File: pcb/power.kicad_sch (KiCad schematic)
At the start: 22 parts, among them U1 74LVC1G08, U12 TPS2121RUXR, U13 TPS2121RUXR, U14 TPS2121RUXR

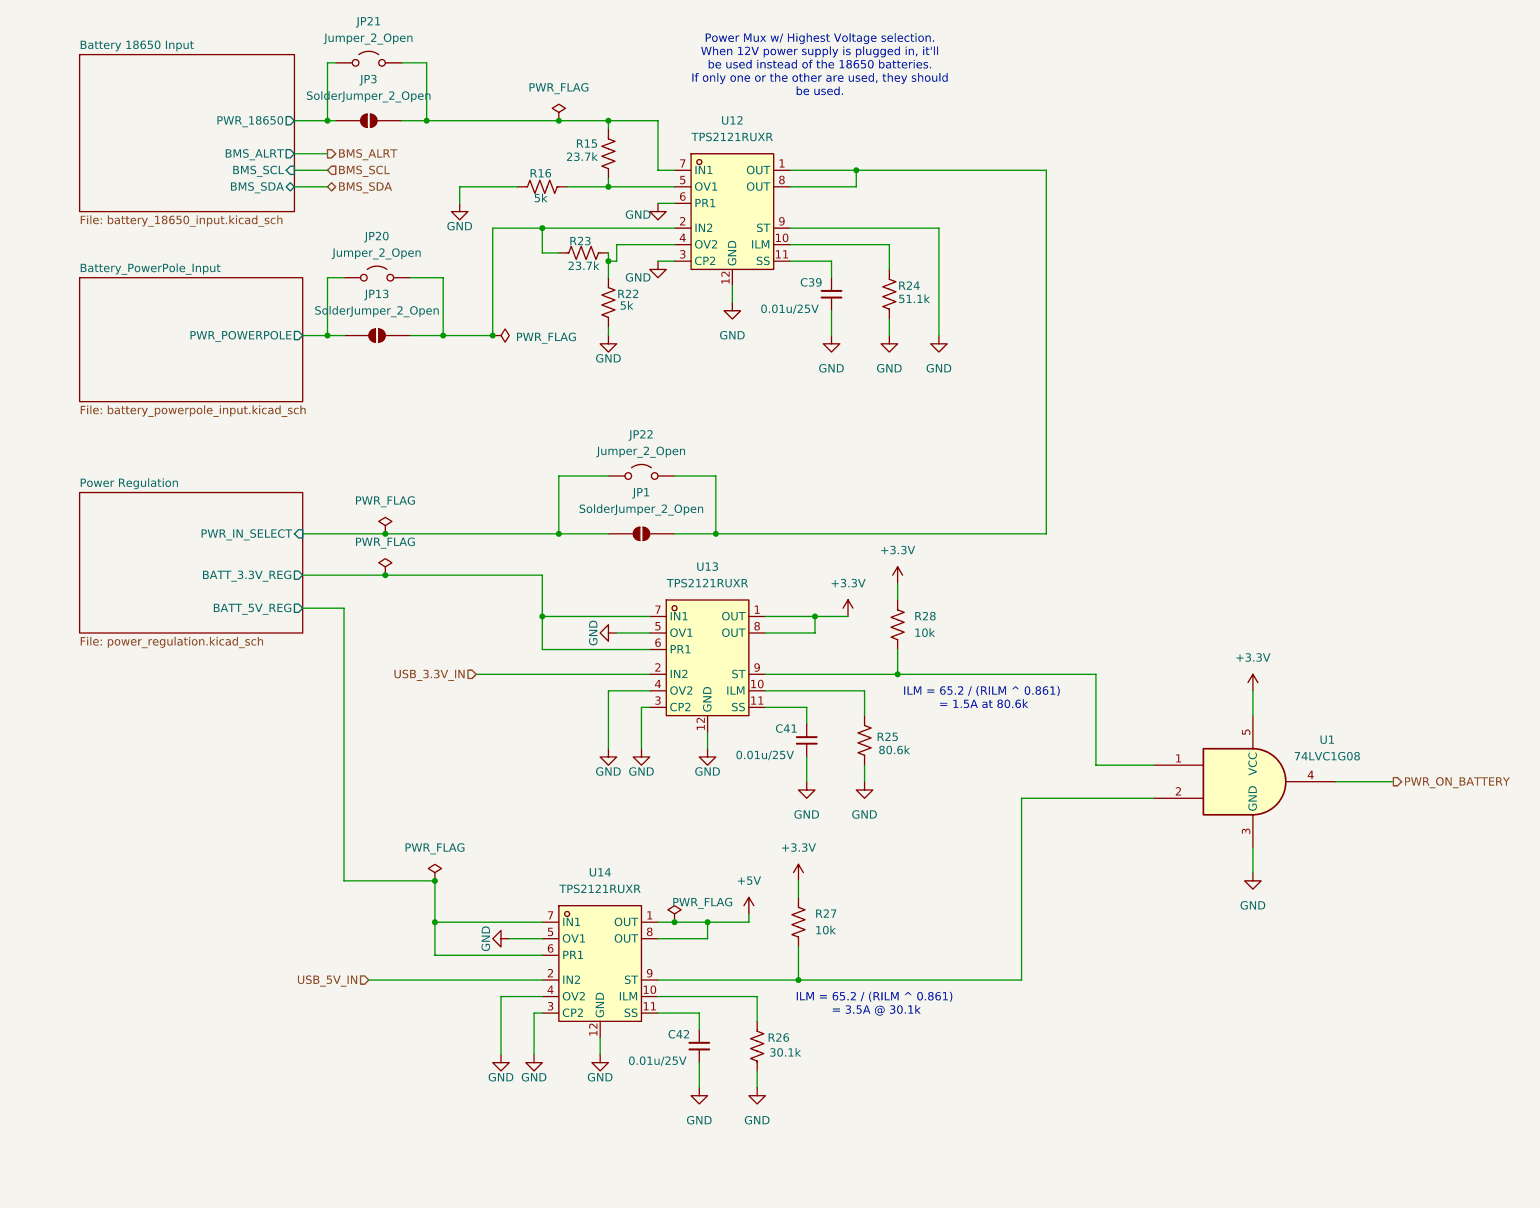
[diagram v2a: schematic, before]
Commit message: Full re-annotation, BOM audit fixes, Stage-1 ILM resize, and PCB reset
Schematic: re-annotated reference designators project-wide (3rd pass) --
every real component's designator has shifted since the last commit.
Fixed BOM gaps found by the fresh audit: U13 (CH340C) sourcing fields,
R7's Manf typo (YAGE -> YAGEO), R5/R8/R14 missing LCSC Part#s, and
normalized U1/U2/U3 (TPS2121RUXR) field names from easyeda2kicad's
defaults (Manufacturer/LCSC Part) to this project's convention
(Manf/LCSC Part #). Resized Stage 1's ILM resistor (R8) from 51.1k to
30.1k -- the prior value undersized the current limit for carrying both
downstream rails' combined battery-side current.

pcb/foxhunt1.kicad_pcb: cleared all footprints. No board layout has
started yet; this reflects that accurately rather than carrying stale
placements from before the schematic settled.

_agent_tasks/bom_property_audit.md: new reusable playbook for this BOM
audit (method, standing exceptions, reporting format), so future passes
don't have to re-derive the approach each time.

_docs/sourcing/task1_lcsc_crossreference.md: replaced stale results
(referencing pre-renumbering designators) with the current audit's
findings. One open item remains: the current-sense shunt's footprint
implies Vishay pad geometry but the sourced part is Milliohm-brand,
needs physical verification before fab.

Co-Authored-By: Claude Sonnet 5 <noreply@anthropic.com>
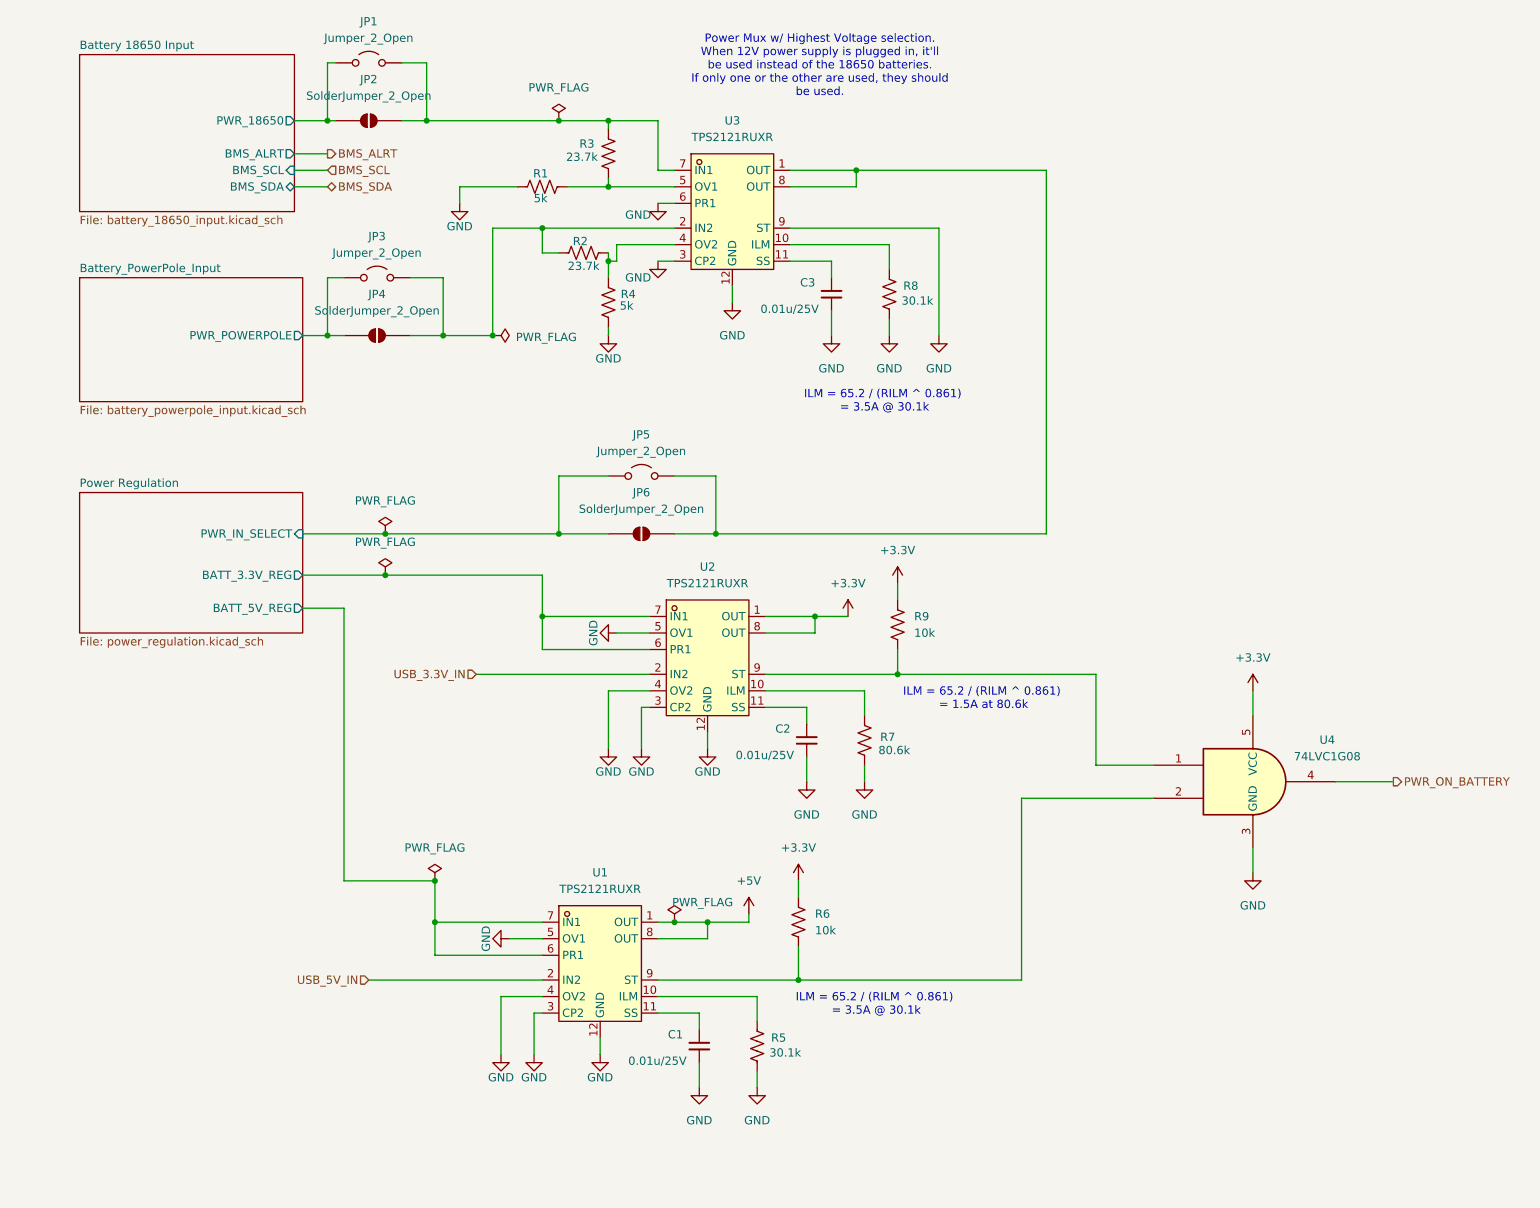
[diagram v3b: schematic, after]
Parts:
- removed R24: 51.1k, Resistor_SMD:R_0201_0603Metric, symbol Device:R_US
- added R8: 30.1k, Resistor_SMD:R_0603_1608Metric, symbol Device:R_US
- JP1: renamed from JP21; footprint (none) -> TestPoint:TestPoint_2Pads_Pitch2.54mm_Drill0.8mm
- JP3: renamed from JP20; footprint (none) -> TestPoint:TestPoint_2Pads_Pitch2.54mm_Drill0.8mm
- JP5: renamed from JP22; footprint (none) -> TestPoint:TestPoint_2Pads_Pitch2.54mm_Drill0.8mm
- R5: renamed from R26; footprint Resistor_SMD:R_0201_0603Metric -> Resistor_SMD:R_0603_1608Metric; LCSC Part # (none) -> C137745; MPN (none) -> RC0603FR-0730K1L; Manf YAGE -> YAGEO
- R7: renamed from R25; footprint Resistor_SMD:R_0201_0603Metric -> Resistor_SMD:R_0603_1608Metric; LCSC Part # (none) -> C862291; MPN (none) -> RT0603BRE0780K6L; Manf YAGE -> YAGEO
- U1: renamed from U14; LCSC Part C485916 -> (none); LCSC Part # (none) -> C485916; Manf (none) -> TI; Manufacturer TI -> (none)
- U2: renamed from U13; LCSC Part C485916 -> (none); LCSC Part # (none) -> C485916; Manf (none) -> TI; Manufacturer TI -> (none)
- U3: renamed from U12; LCSC Part C485916 -> (none); LCSC Part # (none) -> C485916; Manf (none) -> TI; Manufacturer TI -> (none)
- renumbered C42 to C1, C41 to C2, C39 to C3, JP3 to JP2, JP13 to JP4, JP1 to JP6, R16 to R1, R23 to R2, R15 to R3, R22 to R4, R27 to R6, R28 to R9, U1 to U4
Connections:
- net GND: now also R8.1
- net at U3.10 (ILM): now also R8.2

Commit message: Add VRAW soft-latch power switch and MCU/RTC wake network
- Q5 (AO3407A P-FET) gates VRAW into Power Regulation, gate driven by
  a shared active-low wake node (button SW3, RTC_PWR_INTERRUPT,
  MCU_OUT_PWR_LATCH) pulled up to VRAW through 1M R29
- Q6 (BSS138) on the mcu-esp32 sheet lets GPIO48 hold the latch from
  a 3.3V-safe domain without exposing the MCU to VRAW voltage
- JP5/JP6 bench-isolation jumpers in the VRAW-gated path, bridged via
  new VRAW_GATED net label into Power Regulation's PWR_IN_SELECT
- JP24 lets USB be excluded from the TPS2121 power muxes for bench
  testing the sleep/wake cycle while still connected over USB-C
- Added blank Peripherals sheet (mcu-esp32 child) with RTC-facing
  pins stubbed and wired at the root, ready for the PCF8563 circuit
- regulation.md updated for the final 6.67V/4.78V intermediate
  voltages and matched-tolerance thin-film feedback dividers
- open_items.md: added power-off path as a follow-up (latch only
  handles power-on today)

Co-Authored-By: Claude Sonnet 5 <noreply@anthropic.com>
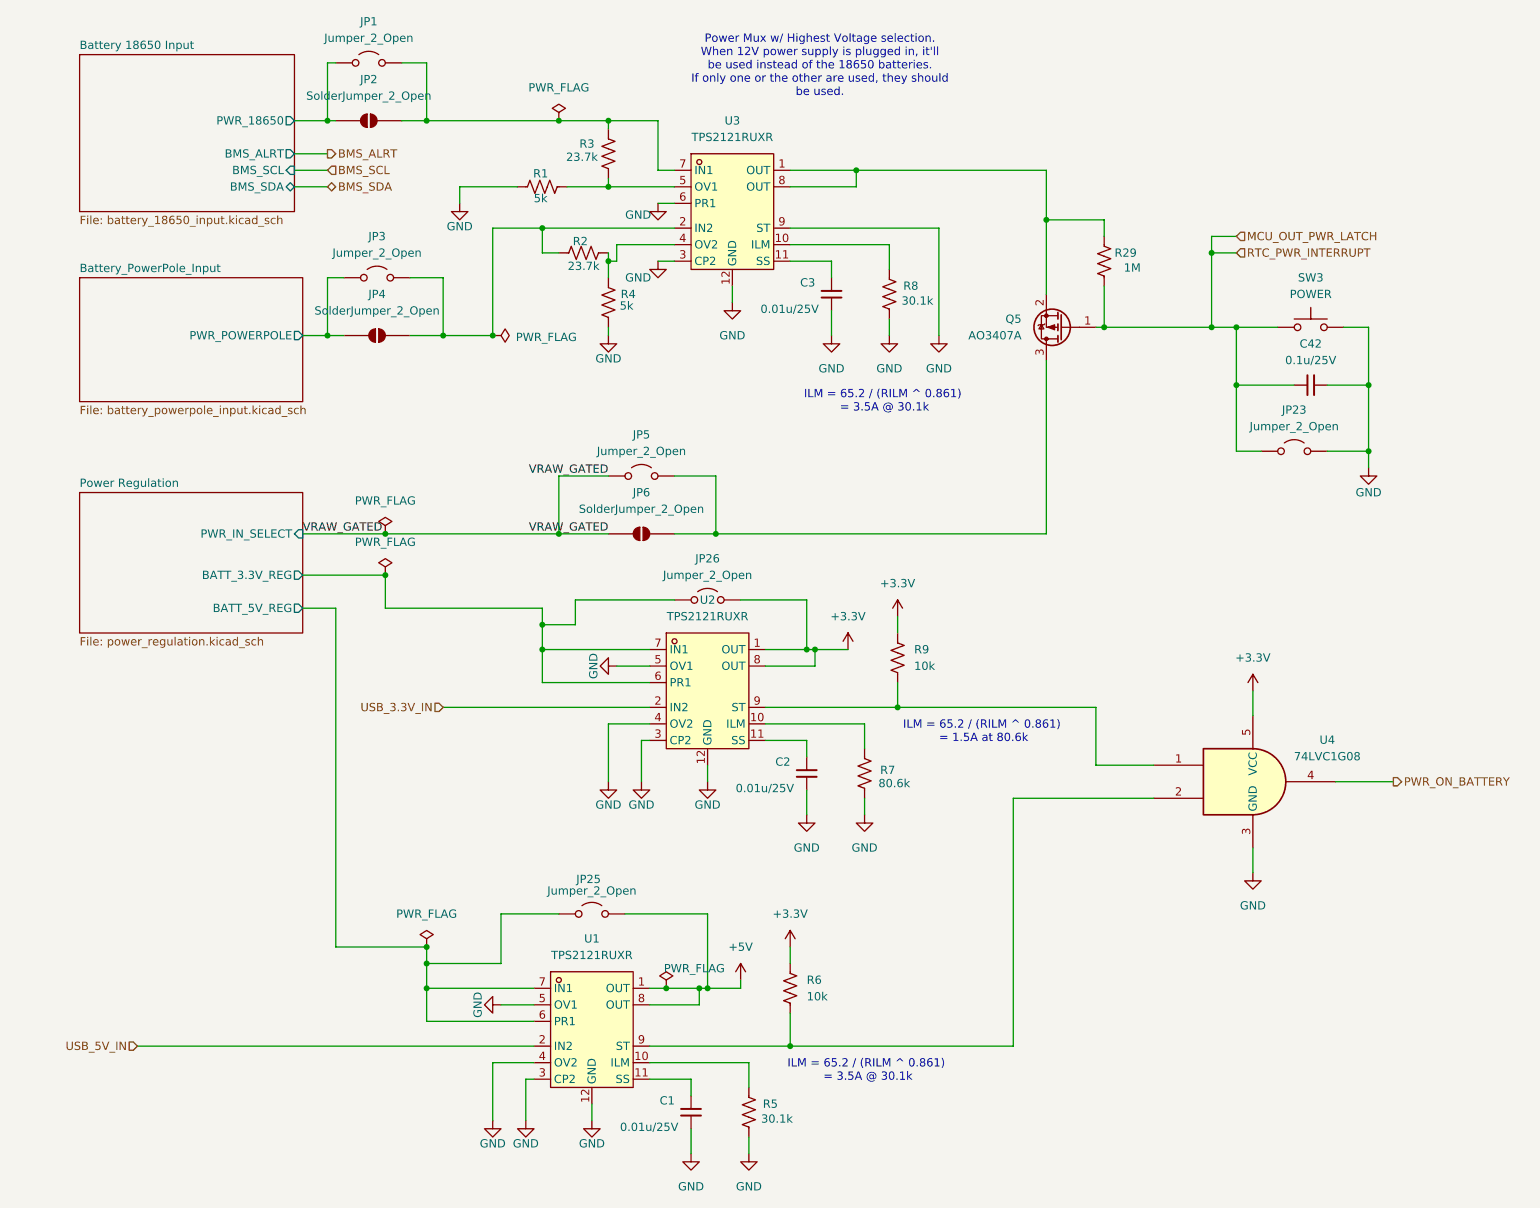
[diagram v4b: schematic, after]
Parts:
- added C42: 0.1u/25V, Capacitor_SMD:C_0603_1608Metric, symbol Device:C_Small
- added JP23, JP25, JP26: Jumper_2_Open, TestPoint:TestPoint_2Pads_Pitch2.54mm_Drill0.8mm, symbol Jumper:Jumper_2_Open
- added Q5: AO3407A, Package_TO_SOT_SMD:SOT-23, symbol Transistor_FET:AO3401A
- added R29: 1M, Resistor_SMD:R_0603_1608Metric, symbol Device:R_US
- added SW3: POWER, Button_Switch_SMD:SW_SPST_PTS645Sx43SMTR92, symbol Switch:SW_Push
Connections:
- net +3.3V: now also JP26.2 (B)
- net +5V: now also JP25.2 (B)
- net GND: now also C42.2, JP23.2 (B), SW3.1
- net Power Regulation/BATT_3.3V_REG: now also JP26.1 (A)
- net Power Regulation/BATT_5V_REG: now also JP25.1 (A)
- net at JP5.2 (B), JP6.2 (B): now also Q5.3 (D); no longer U3.1 (OUT), U3.8 (OUT)
- net Power Regulation/PWR_IN_SELECT renamed VRAW_GATED
- new net: Q5.2 (S), R29.2, U3.1 (OUT), U3.8 (OUT)
- new net MCU_OUT_PWR_LATCH: C42.1, JP23.1 (A), Q5.1 (G), R29.1, SW3.2
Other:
- moved on the sheet: C1, C2, R5, R6, R7, R9, U1, U2
